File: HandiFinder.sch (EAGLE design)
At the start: 25 parts, among them IC2 4047D, X1 SMA-142-0701-801/806

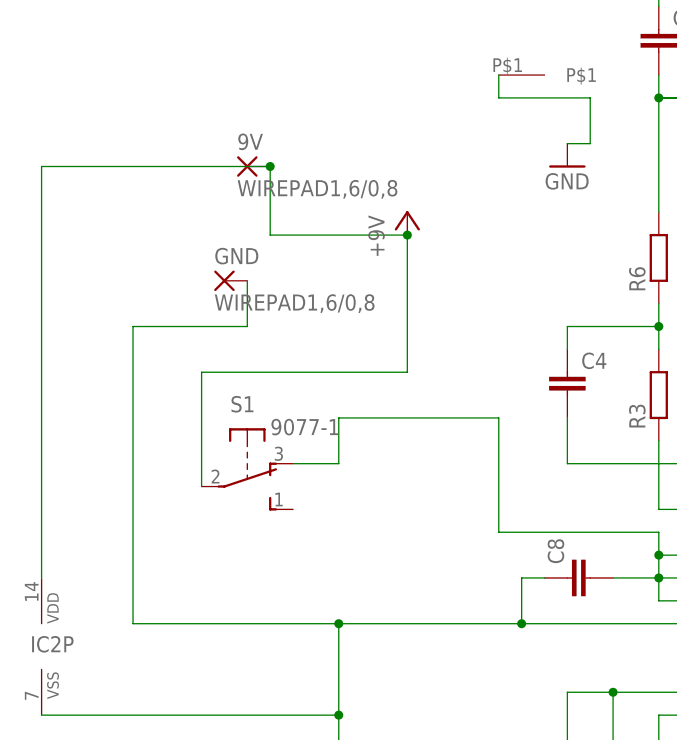
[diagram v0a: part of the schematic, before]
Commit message: Fix switch misconnection.
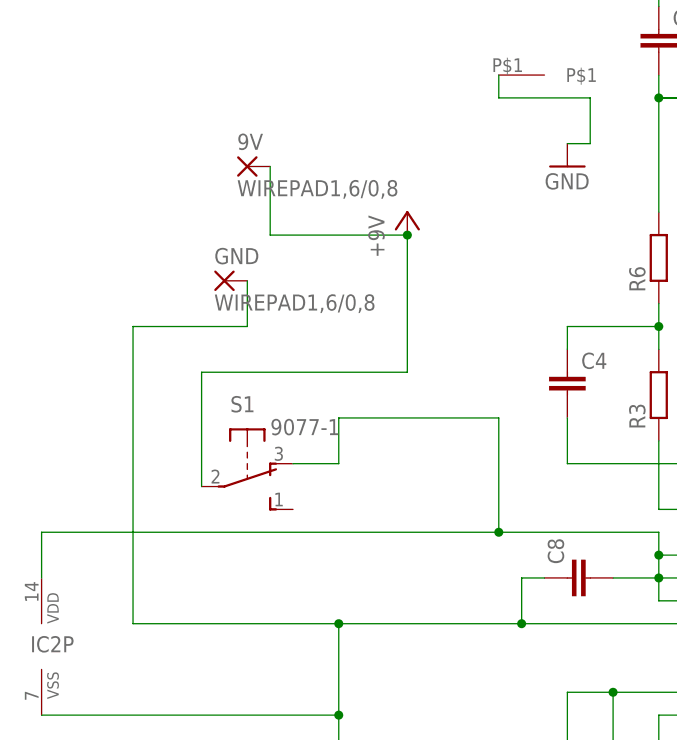
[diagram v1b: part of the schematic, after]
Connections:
- net +5V: no longer IC2P.VDD
- net N$16: now also IC2P.VDD
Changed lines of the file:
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@@
 <wire x1="2.54" y1="58.42" x2="17.78" y2="58.42" width="0.1524" layer="91"/>
 <junction x="17.78" y="58.42"/>
-<pinref part="IC2" gate="P" pin="VDD"/>
-<wire x1="-22.86" y1="20.32" x2="-22.86" y2="66.04" width="0.1524" layer="91"/>
-<wire x1="-22.86" y1="66.04" x2="2.54" y2="66.04" width="0.1524" layer="91"/>
-<junction x="2.54" y="66.04"/>
 <pinref part="S1" gate="1" pin="P"/>
 <wire x1="-5.08" y1="30.48" x2="-5.08" y2="43.18" width="0.1524" layer="91"/>
@@
 <pinref part="S1" gate="1" pin="O"/>
 <wire x1="5.08" y1="33.02" x2="10.16" y2="33.02" width="0.1524" layer="91"/>
+<pinref part="IC2" gate="P" pin="VDD"/>
+<wire x1="-22.86" y1="20.32" x2="-22.86" y2="25.4" width="0.1524" layer="91"/>
+<wire x1="-22.86" y1="25.4" x2="27.94" y2="25.4" width="0.1524" layer="91"/>
+<junction x="27.94" y="25.4"/>
 </segment>
 </net>
